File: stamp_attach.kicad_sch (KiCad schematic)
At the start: 1 part, among them J1 TOP

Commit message: updated footprints with oval pads; added solder points for bottom PCB
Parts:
- J1: footprint Stamp_Attach:SA_top_layer -> Stamp_Attach:SA_layer_A
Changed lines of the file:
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@@
     (property "Reference" "J1" (id 0) (at 175.26 57.15 0))
     (property "Value" "TOP" (id 1) (at 175.26 59.69 0))
-    (property "Footprint" "Stamp_Attach:SA_top_layer" (id 2) (at 173.99 66.04 0)
+    (property "Footprint" "Stamp_Attach:SA_layer_A" (id 2) (at 173.99 66.04 0)
       (effects (font (size 1.27 1.27)) hide)
     )
@@
   (symbol_instances
     (path "/60dcd1fe-7079-4cb8-b509-04558ccf5097"
-      (reference "J1") (unit 1) (value "TOP") (footprint "Stamp_Attach:SA_top_layer")
+      (reference "J1") (unit 1) (value "TOP") (footprint "Stamp_Attach:SA_layer_A")
     )
   )

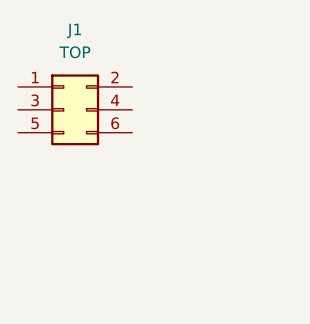
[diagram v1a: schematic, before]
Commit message: updated footprints; changed pads to be 0.25mm spacing and clearance; made the mounting holes PTH with custom pad
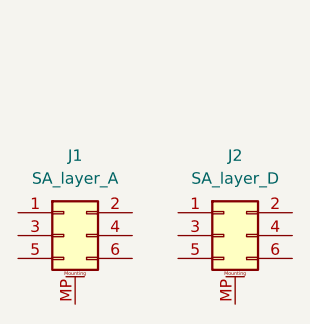
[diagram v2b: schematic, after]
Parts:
- removed J1: TOP, Stamp_Attach:SA_layer_A, symbol Connector_Generic:Conn_02x03_Odd_Even
- added J1: SA_layer_A, Stamp_Attach:SA_layer_A, symbol Connector_Generic_MountingPin:Conn_02x03_Odd_Even_MountingPin
- added J2: SA_layer_D, Stamp_Attach:SA_layer_D, symbol Connector_Generic_MountingPin:Conn_02x03_Odd_Even_MountingPin
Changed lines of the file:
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@@
 (kicad_sch (version 20211123) (generator eeschema)
   (paper "A4")
-  (symbol (lib_id "Connector_Generic:Conn_02x03_Odd_Even") (at 173.99 66.04 0) (unit 1)
+  (symbol (lib_id "Connector_Generic_MountingPin:Conn_02x03_Odd_Even_MountingPin") (at 173.99 80.01 0) (unit 1)
     (in_bom yes) (on_board yes) (fields_autoplaced)
-    (property "Reference" "J1" (id 0) (at 175.26 57.15 0))
-    (property "Value" "TOP" (id 1) (at 175.26 59.69 0))
-    (property "Footprint" "Stamp_Attach:SA_layer_A" (id 2) (at 173.99 66.04 0)
+    (property "Reference" "J1" (id 0) (at 175.26 71.12 0))
+    (property "Value" "SA_layer_A" (id 1) (at 175.26 73.66 0))
+    (property "Footprint" "Stamp_Attach:SA_layer_A" (id 2) (at 173.99 80.01 0)
       (effects (font (size 1.27 1.27)) hide)
     )
-    (property "Datasheet" "~" (id 3) (at 173.99 66.04 0)
+    (property "Datasheet" "~" (id 3) (at 173.99 80.01 0)
       (effects (font (size 1.27 1.27)) hide)
     )
@@
     (pin "5")
     (pin "6")
+    (pin "MP")
+  )
+  (symbol (lib_id "Connector_Generic_MountingPin:Conn_02x03_Odd_Even_MountingPin") (at 191.77 80.01 0) (unit 1)
+    (in_bom yes) (on_board yes) (fields_autoplaced)
+    (property "Reference" "J2" (id 0) (at 193.04 71.12 0))
+    (property "Value" "SA_layer_D" (id 1) (at 193.04 73.66 0))
+    (property "Footprint" "Stamp_Attach:SA_layer_D" (id 2) (at 191.77 80.01 0)
+      (effects (font (size 1.27 1.27)) hide)
+    )
+    (property "Datasheet" "~" (id 3) (at 191.77 80.01 0)
+      (effects (font (size 1.27 1.27)) hide)
+    )
+    (pin "1")
+    (pin "2")
+    (pin "3")
+    (pin "4")
+    (pin "5")
+    (pin "6")
+    (pin "MP")
   )
   (sheet_instances
@@
   )
   (symbol_instances
-    (path "/60dcd1fe-7079-4cb8-b509-04558ccf5097"
-      (reference "J1") (unit 1) (value "TOP") (footprint "Stamp_Attach:SA_layer_A")
+    (path "/41485de5-6ed3-4c83-b69e-ef83ae18093c"
+      (reference "J1") (unit 1) (value "SA_layer_A") (footprint "Stamp_Attach:SA_layer_A")
+    )
+    (path "/d541c241-6514-4616-8a13-b9e39e22f5ed"
+      (reference "J2") (unit 1) (value "SA_layer_D") (footprint "Stamp_Attach:SA_layer_D")
     )
   )

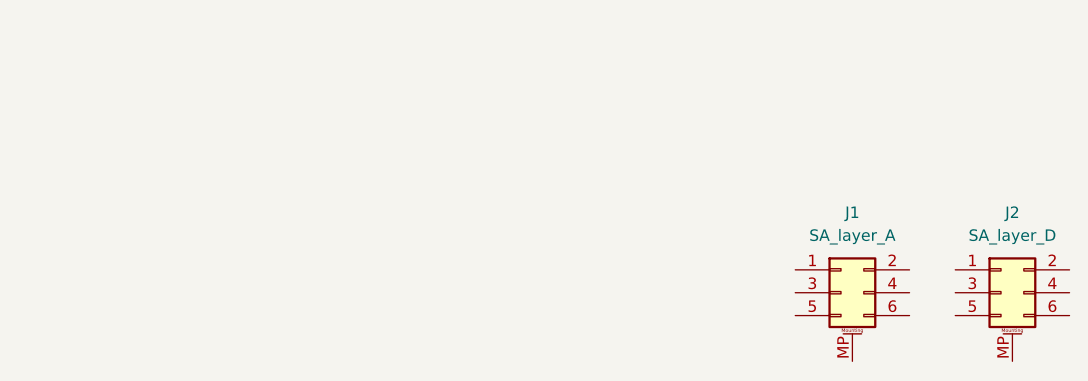
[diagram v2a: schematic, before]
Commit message: completed graphics area of info card
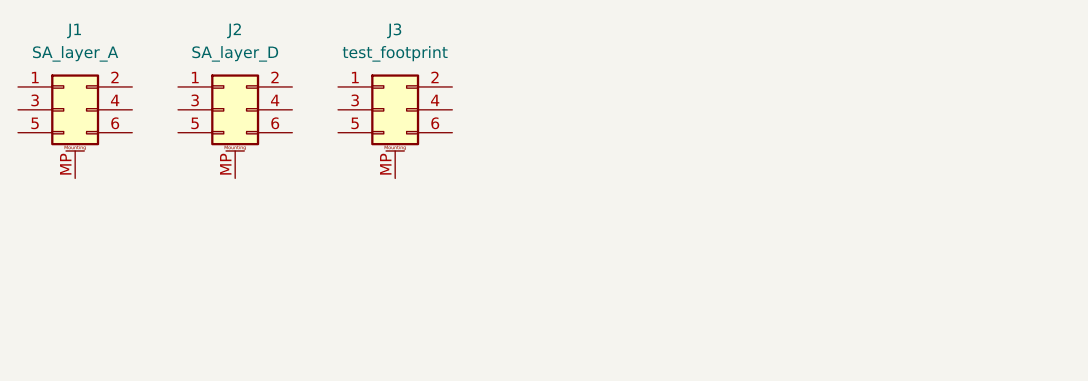
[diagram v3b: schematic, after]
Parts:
- added J3: test_footprint, Stamp_Attach:Test_Footprint, symbol Connector_Generic_MountingPin:Conn_02x03_Odd_Even_MountingPin
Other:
- moved on the sheet: J1, J2
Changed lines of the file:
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@@
 (kicad_sch (version 20211123) (generator eeschema)
-  (paper "A4")
-  (symbol (lib_id "Connector_Generic_MountingPin:Conn_02x03_Odd_Even_MountingPin") (at 173.99 80.01 0) (unit 1)
+  (paper "A5")
+  (symbol (lib_id "Connector_Generic_MountingPin:Conn_02x03_Odd_Even_MountingPin") (at 87.63 59.69 0) (unit 1)
     (in_bom yes) (on_board yes) (fields_autoplaced)
-    (property "Reference" "J1" (id 0) (at 175.26 71.12 0))
-    (property "Value" "SA_layer_A" (id 1) (at 175.26 73.66 0))
-    (property "Footprint" "Stamp_Attach:SA_layer_A" (id 2) (at 173.99 80.01 0)
+    (property "Reference" "J1" (id 0) (at 88.9 50.8 0))
+    (property "Value" "SA_layer_A" (id 1) (at 88.9 53.34 0))
+    (property "Footprint" "Stamp_Attach:SA_layer_A" (id 2) (at 87.63 59.69 0)
       (effects (font (size 1.27 1.27)) hide)
     )
-    (property "Datasheet" "~" (id 3) (at 173.99 80.01 0)
+    (property "Datasheet" "~" (id 3) (at 87.63 59.69 0)
       (effects (font (size 1.27 1.27)) hide)
     )
@@
     (pin "MP")
   )
-  (symbol (lib_id "Connector_Generic_MountingPin:Conn_02x03_Odd_Even_MountingPin") (at 191.77 80.01 0) (unit 1)
+  (symbol (lib_id "Connector_Generic_MountingPin:Conn_02x03_Odd_Even_MountingPin") (at 105.41 59.69 0) (unit 1)
     (in_bom yes) (on_board yes) (fields_autoplaced)
-    (property "Reference" "J2" (id 0) (at 193.04 71.12 0))
-    (property "Value" "SA_layer_D" (id 1) (at 193.04 73.66 0))
-    (property "Footprint" "Stamp_Attach:SA_layer_D" (id 2) (at 191.77 80.01 0)
+    (property "Reference" "J2" (id 0) (at 106.68 50.8 0))
+    (property "Value" "SA_layer_D" (id 1) (at 106.68 53.34 0))
+    (property "Footprint" "Stamp_Attach:SA_layer_D" (id 2) (at 105.41 59.69 0)
       (effects (font (size 1.27 1.27)) hide)
     )
-    (property "Datasheet" "~" (id 3) (at 191.77 80.01 0)
+    (property "Datasheet" "~" (id 3) (at 105.41 59.69 0)
+      (effects (font (size 1.27 1.27)) hide)
+    )
+    (pin "1")
+    (pin "2")
+    (pin "3")
+    (pin "4")
+    (pin "5")
+    (pin "6")
+    (pin "MP")
+  )
+  (symbol (lib_id "Connector_Generic_MountingPin:Conn_02x03_Odd_Even_MountingPin") (at 123.19 59.69 0) (unit 1)
+    (in_bom yes) (on_board yes) (fields_autoplaced)
+    (property "Reference" "J3" (id 0) (at 124.46 50.8 0))
+    (property "Value" "test_footprint" (id 1) (at 124.46 53.34 0))
+    (property "Footprint" "Stamp_Attach:Test_Footprint" (id 2) (at 123.19 59.69 0)
+      (effects (font (size 1.27 1.27)) hide)
+    )
+    (property "Datasheet" "~" (id 3) (at 123.19 59.69 0)
       (effects (font (size 1.27 1.27)) hide)
     )
@@
       (reference "J2") (unit 1) (value "SA_layer_D") (footprint "Stamp_Attach:SA_layer_D")
     )
+    (path "/e3c3d042-f4c5-4fb1-a6b8-52aa1c14cc0e"
+      (reference "J3") (unit 1) (value "test_footprint") (footprint "Stamp_Attach:Test_Footprint")
+    )
   )
